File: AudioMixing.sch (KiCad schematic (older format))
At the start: 34 parts

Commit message: Mehr Hierarchie
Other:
- note removed: "Signal müssen noch global\noder hirarschisch gemacht werden"
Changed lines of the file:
@@
 $Descr A4 11693 8268
 encoding utf-8
-Sheet 5 5
+Sheet 5 7
 Title ""
 Date ""
@@
 	3650 5300 3500 5300
 Wire Notes Line
-	4300 5150 3500 5150
-Wire Notes Line
-	3500 5150 3500 6650
-Wire Notes Line
-	3500 6650 4300 6650
-Wire Notes Line
-	4300 6650 4300 5150
-Wire Notes Line
 	10000 1950 10800 1950
 Wire Notes Line
@@
 Wire Notes Line
 	10000 3100 10000 1950
-Wire Notes Line
-	10100 3800 11050 3800
-Wire Notes Line
-	11050 3800 11050 4500
-Wire Notes Line
-	11050 4500 10100 4500
-Wire Notes Line
-	10100 4500 10100 3800
-Text Notes 11250 4700 1    50   ~ 0
-Signal müssen noch global\noder hirarschisch gemacht werden
 $Comp
 L TeKaDe:MAX98089ETN+ U?

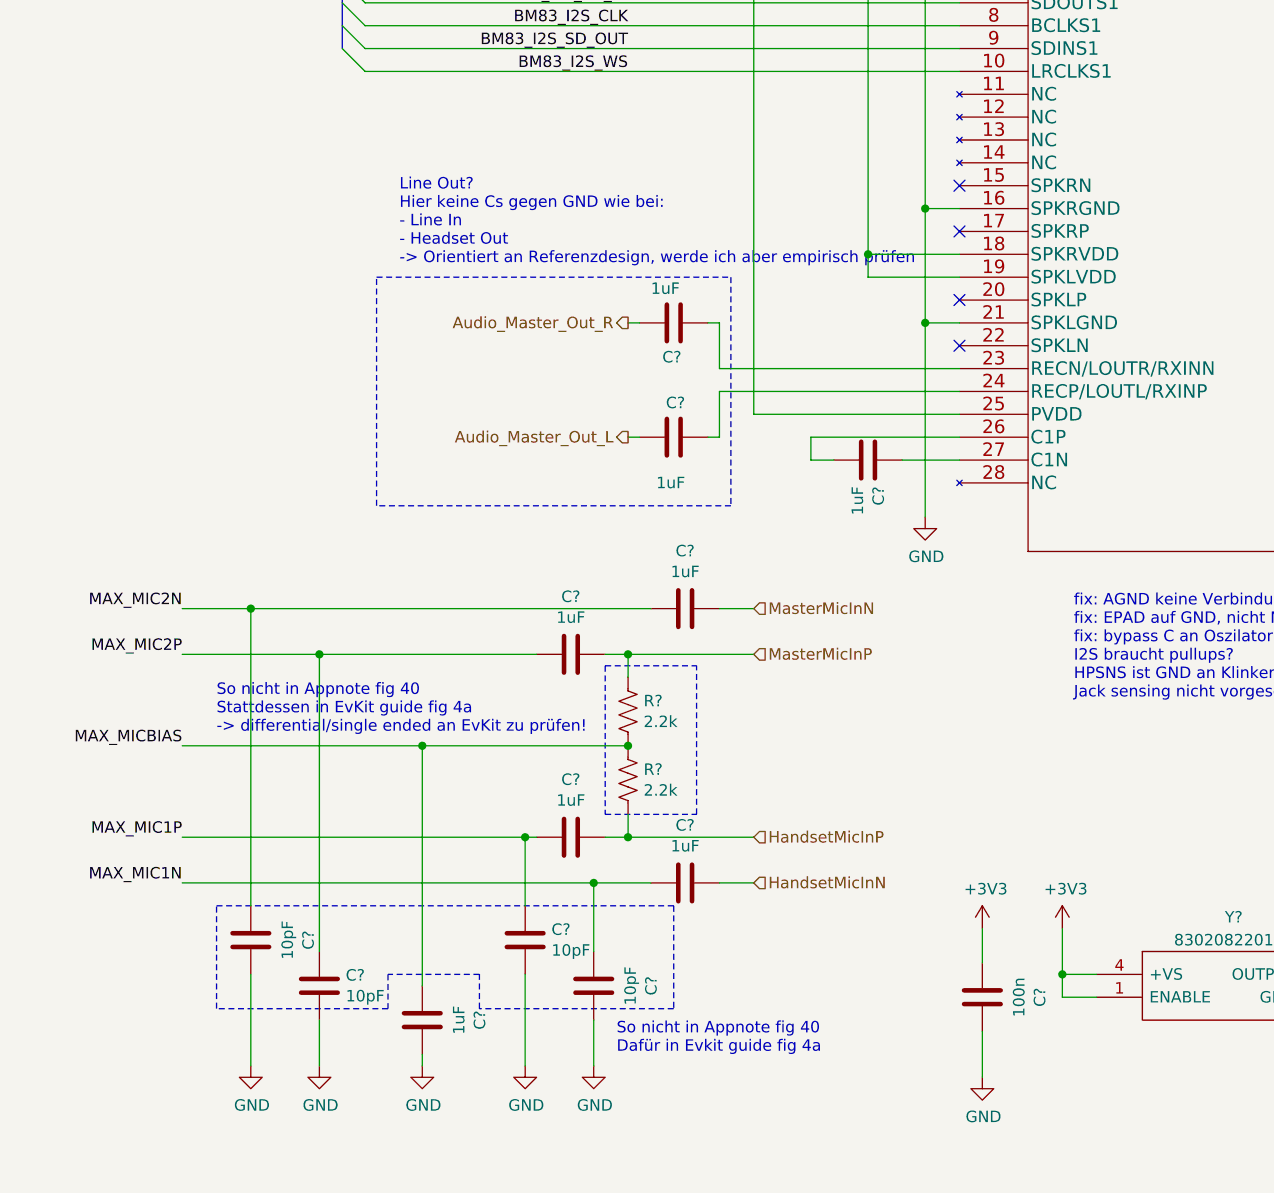
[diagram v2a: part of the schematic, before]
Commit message: [add:] MAX98089 Line Out caps
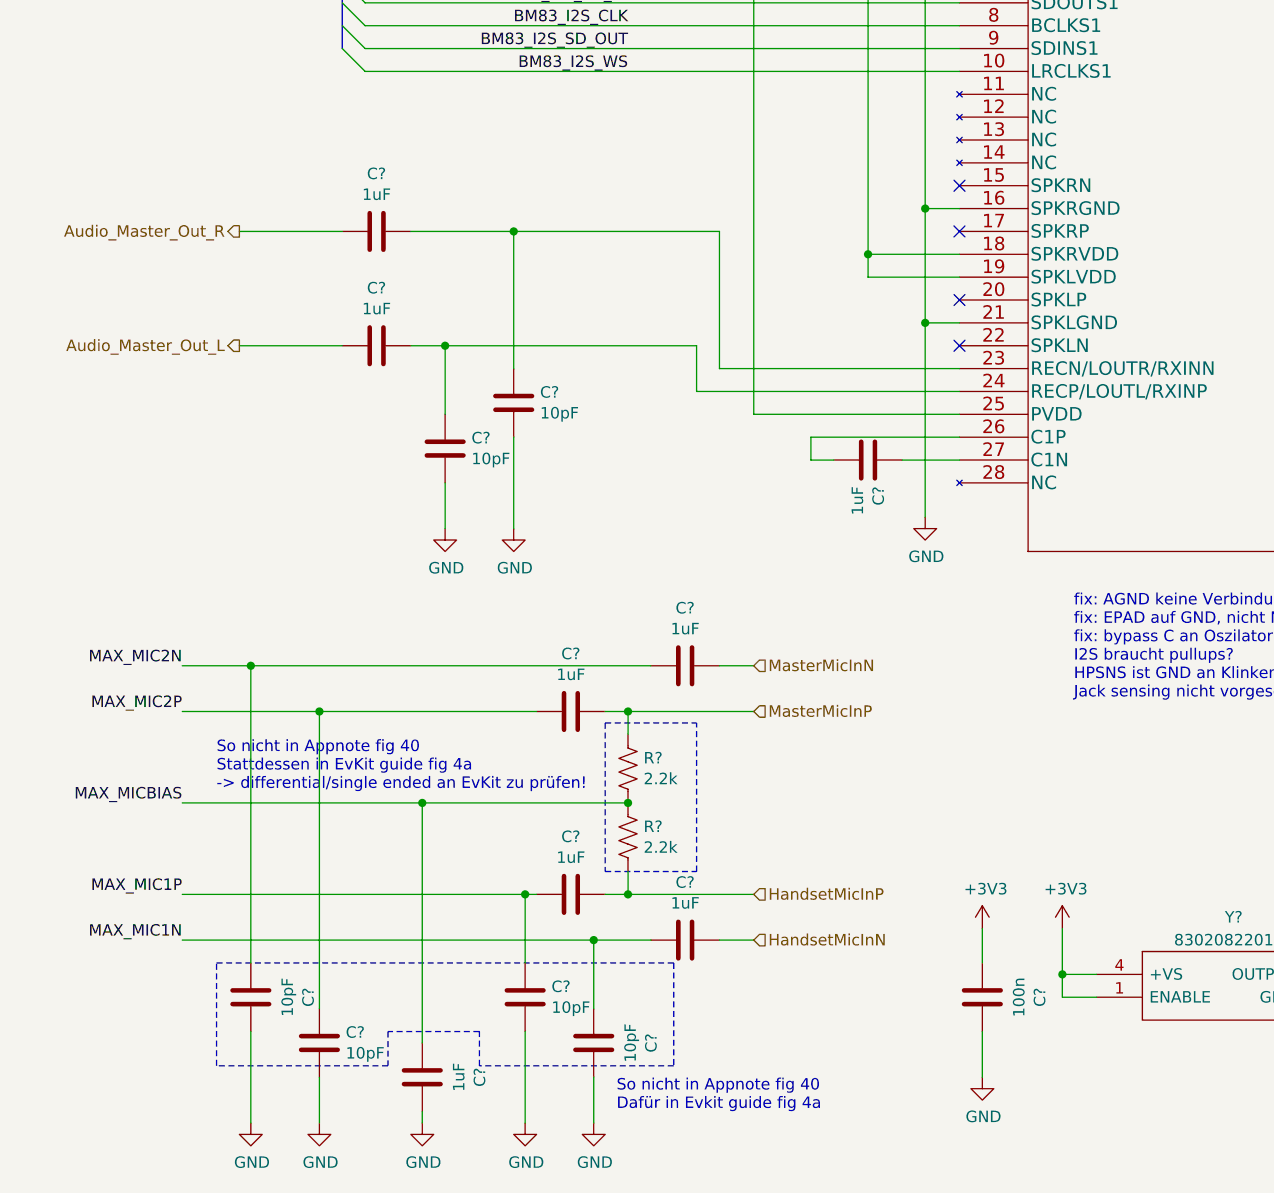
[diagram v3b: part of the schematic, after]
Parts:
- removed C? (x2): 1uF, symbol Device:C
- added C? (x2): 10pF, symbol Device:C
- added C? (x2): 1uF, symbol Device:C
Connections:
- net Audio_Master_Out_L: now also C?.2
- net Audio_Master_Out_R: now also C?.2
- net GND: now also C?.2, C?.2
- net at U?.23 (RECN/LOUTR/RXINN): now also C?.1, C?.1
- net at U?.24 (RECP/LOUTL/RXINP): now also C?.1, C?.1
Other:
- note removed: "Line Out?\nHier keine Cs gegen GND wie bei:\n- Line In\n- Headset Out\n-> Orientiert an Referenzdesign, werde ich aber empirisch prüfen"
- moved on the sheet: C?, R?

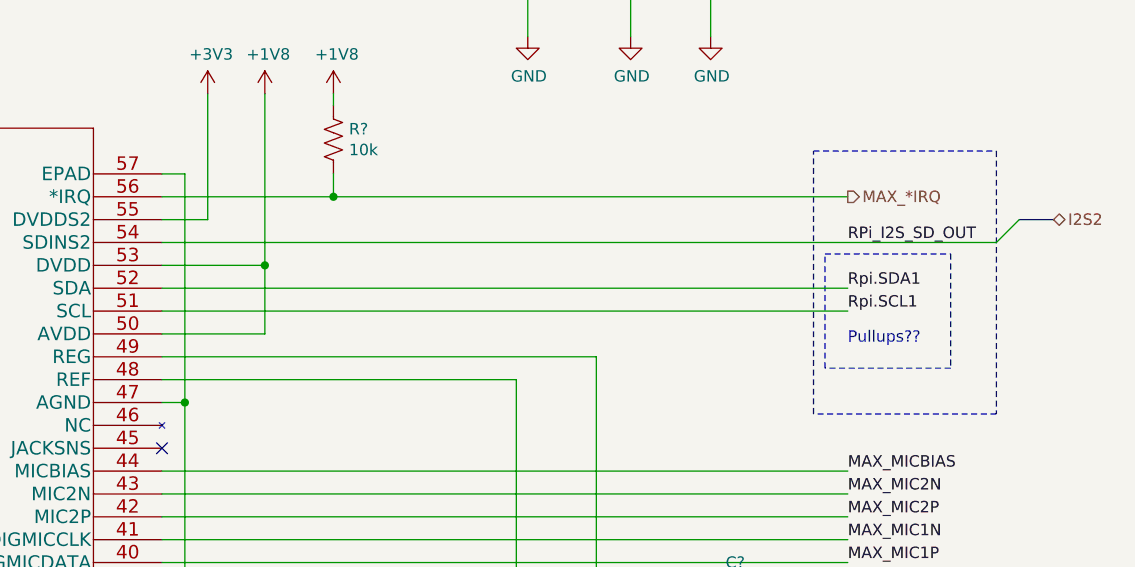
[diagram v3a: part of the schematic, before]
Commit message: [modified:] RPI I2C splitting
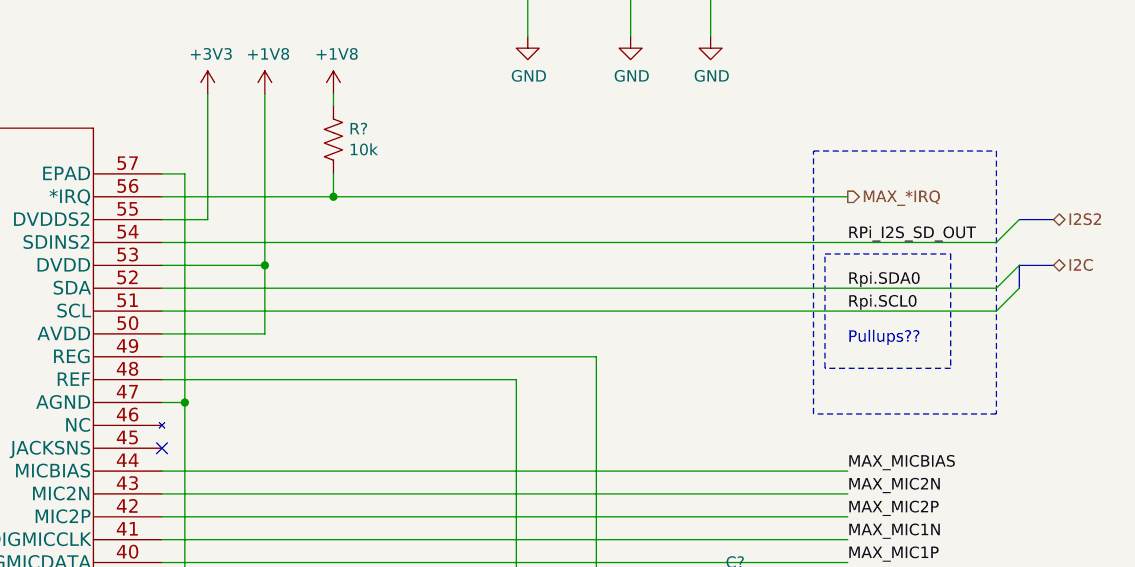
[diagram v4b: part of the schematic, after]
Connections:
- net Rpi.SCL1 renamed Rpi.SCL0
- net Rpi.SDA1 renamed Rpi.SDA0
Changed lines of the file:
@@
 	7900 2150 10150 2150
 Text Label 10150 2550 0    50   ~ 0
-Rpi.SDA1
+Rpi.SDA0
 Text Label 10150 2650 0    50   ~ 0
-Rpi.SCL1
-Wire Wire Line
-	7150 2550 10150 2550
-Wire Wire Line
-	10150 2650 7150 2650
+Rpi.SCL0
 $Comp
 L power:+3V3 #PWR?
@@
 	0    1    1    0
 $EndComp
+Entry Wire Line
+	10900 2550 10800 2650
+Entry Wire Line
+	10900 2450 10800 2550
+Text HLabel 11050 2450 2    50   BiDi ~ 0
+I2C
+Wire Wire Line
+	7150 2650 10800 2650
+Wire Wire Line
+	7150 2550 10800 2550
+Wire Bus Line
+	10900 2550 10900 2450
+Wire Bus Line
+	10900 2450 11050 2450
 Wire Bus Line
 	1850 1950 1850 2250

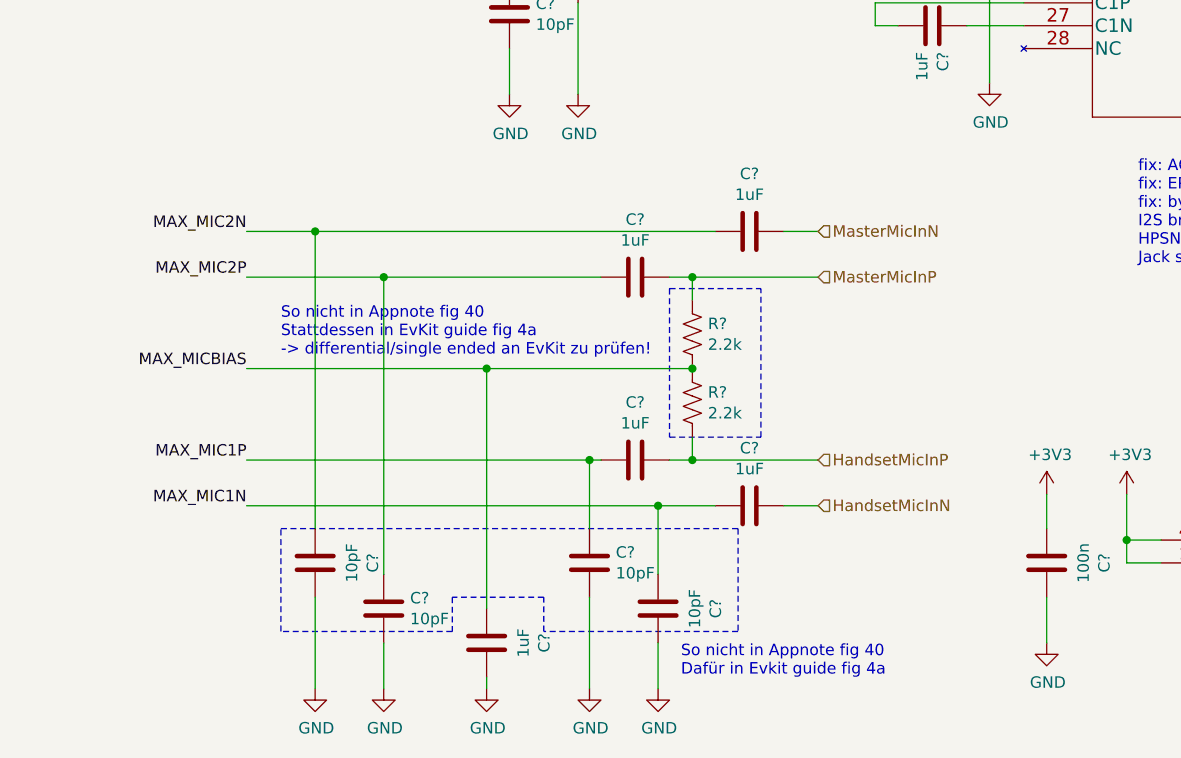
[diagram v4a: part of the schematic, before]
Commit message: [fix:] differential microphone input
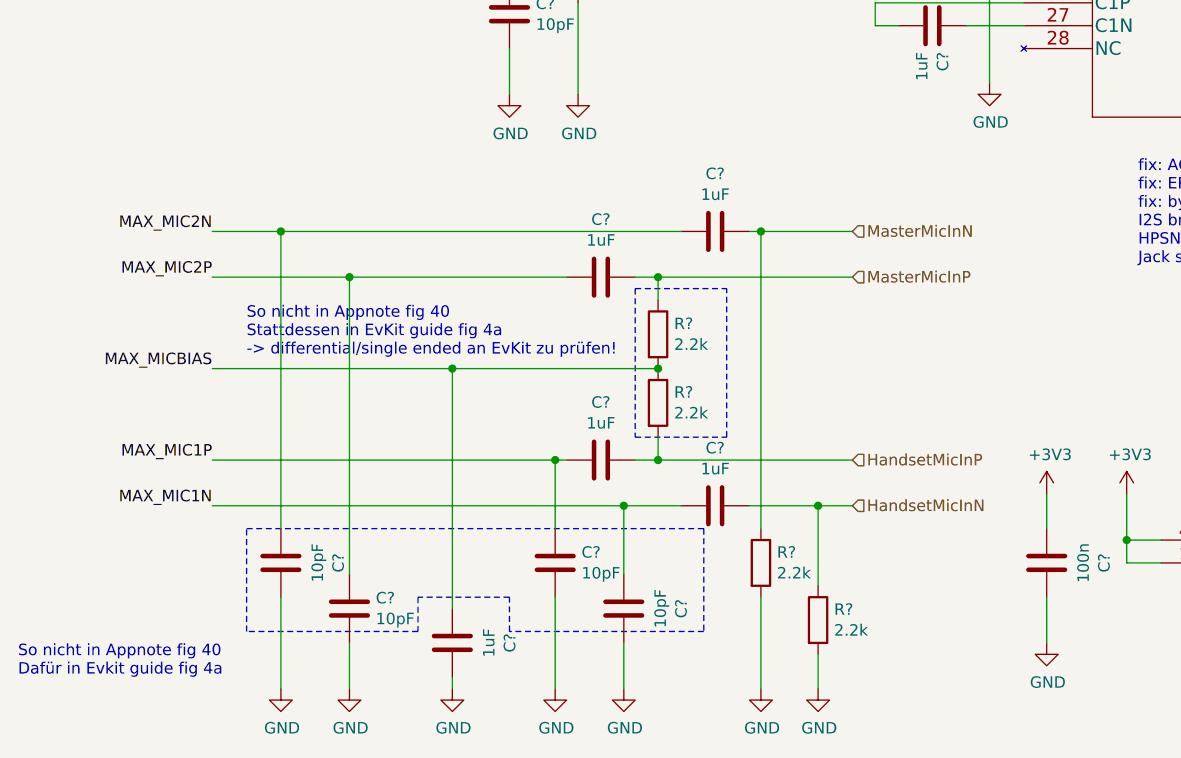
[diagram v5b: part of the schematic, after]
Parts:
- removed R? (x2): 2.2k, symbol Device:R_US
- added R? (x4): 2.2k, symbol Device:R
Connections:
- net GND: now also R?.2, R?.2
- net HandsetMicInN: now also R?.1
- net HandsetMicInP: now also R?.2
- net MAX_MICBIAS: now also R?.1, R?.2
- net MasterMicInN: now also R?.1
- net MasterMicInP: now also R?.1
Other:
- moved on the sheet: C?
